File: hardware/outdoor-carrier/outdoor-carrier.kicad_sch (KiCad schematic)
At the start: 49 parts, among them J1 24 VAC, J2 Mode in 24 VAC, J3 XDB307 liquid, J4 XDB307 vapor, J5 XDB307 t.suction, J6 TH1 suction, J7 TH2 liquid, J8 SHT30 FS400, J9 TH3 t.suction, U1 ESP32 DevKit, U2 LM2596HV, U3 ADS1115 0x48, U4 ADS1115 0x49, U5 H11AA1, U6 H11AA1

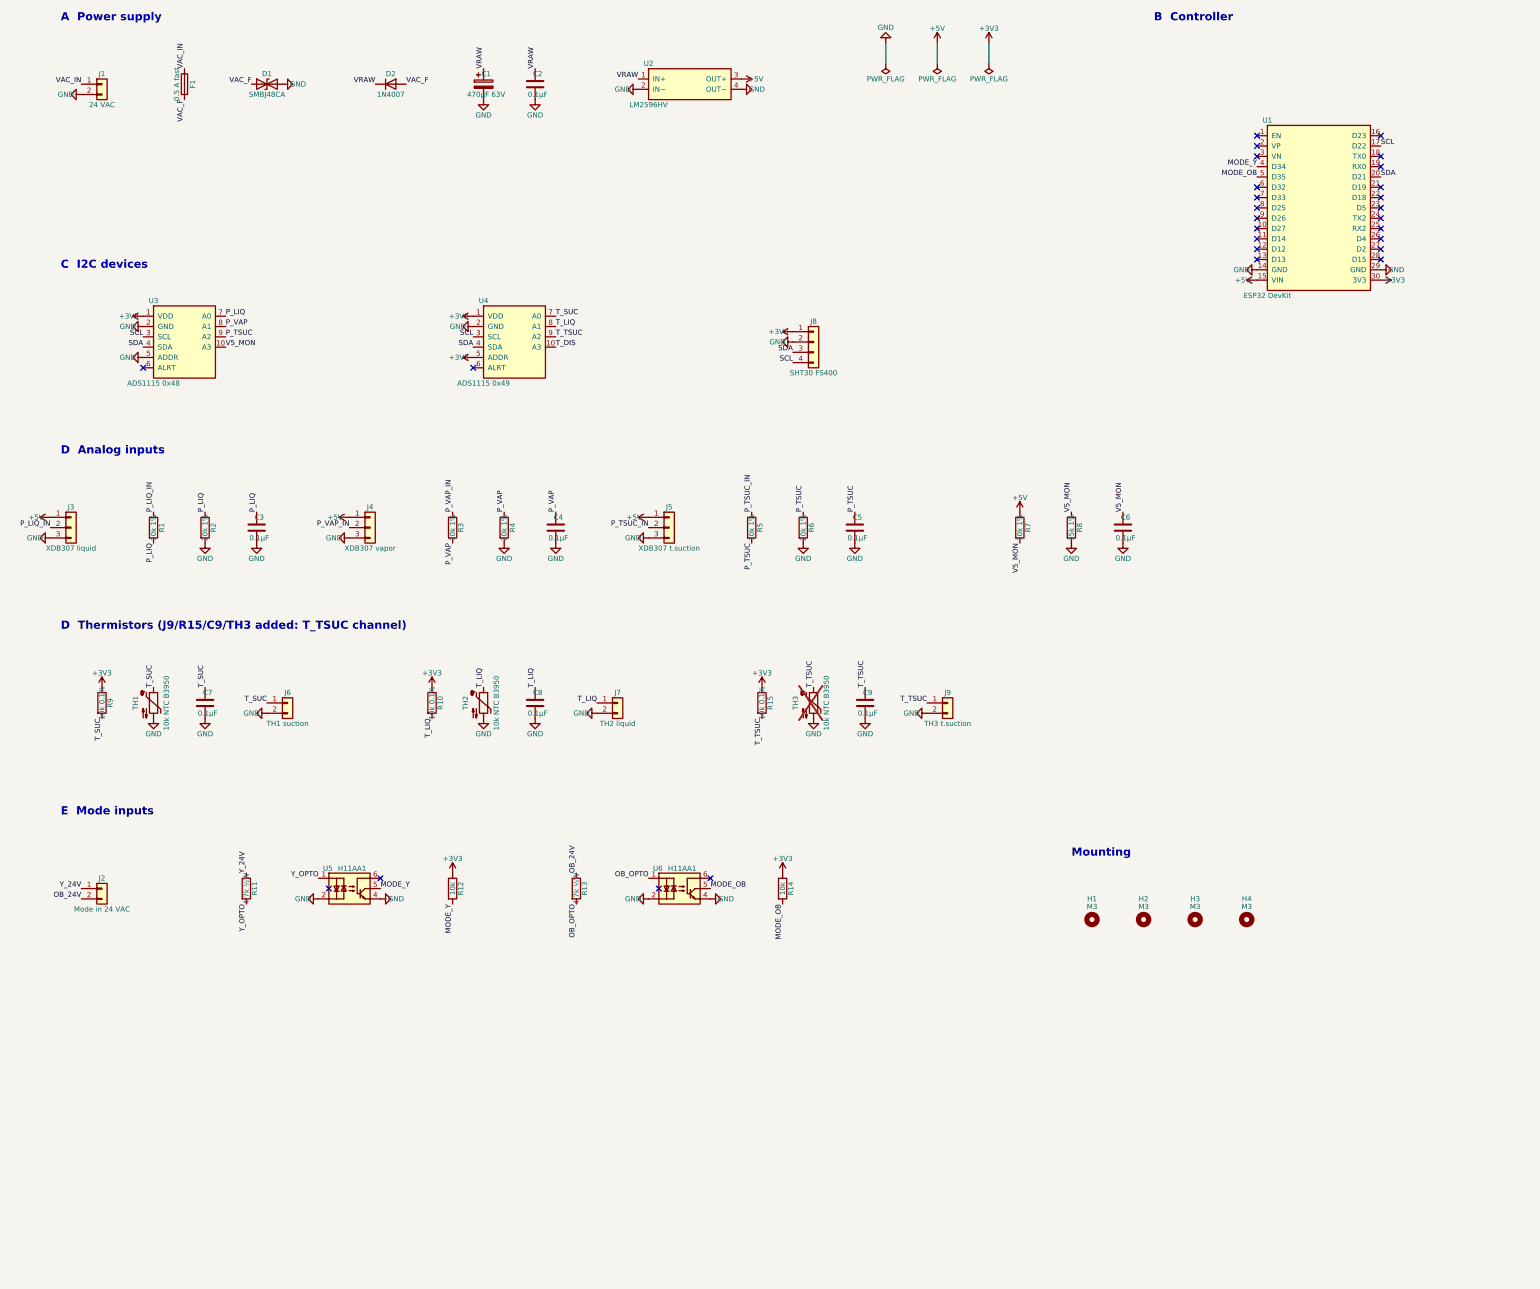
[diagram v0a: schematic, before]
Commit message: Rev B schematics: Wio-SX1262 footprint, flattened AMS1117 symbol, ERC clean
gen_footprints.py: Wio_SX1262 from the Seeed datasheet V1.0 figure 9 (pins 1-8 on
one edge, 12..9 on the other, counter-clockwise; matches design.lora_section and
figure 2). Pads 0.6 x 3.0 mm, 0.8 mm longer outward than the datasheet's 2.2 for hand
soldering; courtyard runs 5 mm past the u.FL side for the plug and pigtail.
gen_sch.py: flatten derived library symbols (AMS1117-3.3 extends AP1117-15), keep
field justification. check_netlist.py: letter pin numbers (audio jack S/T/R) and the
Wio module in the connector summary. design.py: LoRa section spaced out on the sheet.
Checked against KiCad 10: TCA9548APWR pins match MUX_PINS / A0-A2 / RESET / SDA /
SCL / VCC; AudioJack3 S/T/R match the SJ1-3523N pads; AMS1117 1 GND 2 VO 3 VI;
every footprint in design.py exists. ERC 0 errors 0 warnings on both boards.

Co-Authored-By: Claude Opus 5.5 (1M context) <noreply@anthropic.com>
Claude-Session: https://claude.ai/code/session_01V4kWJ9CiBrt94u4WqUxFsk
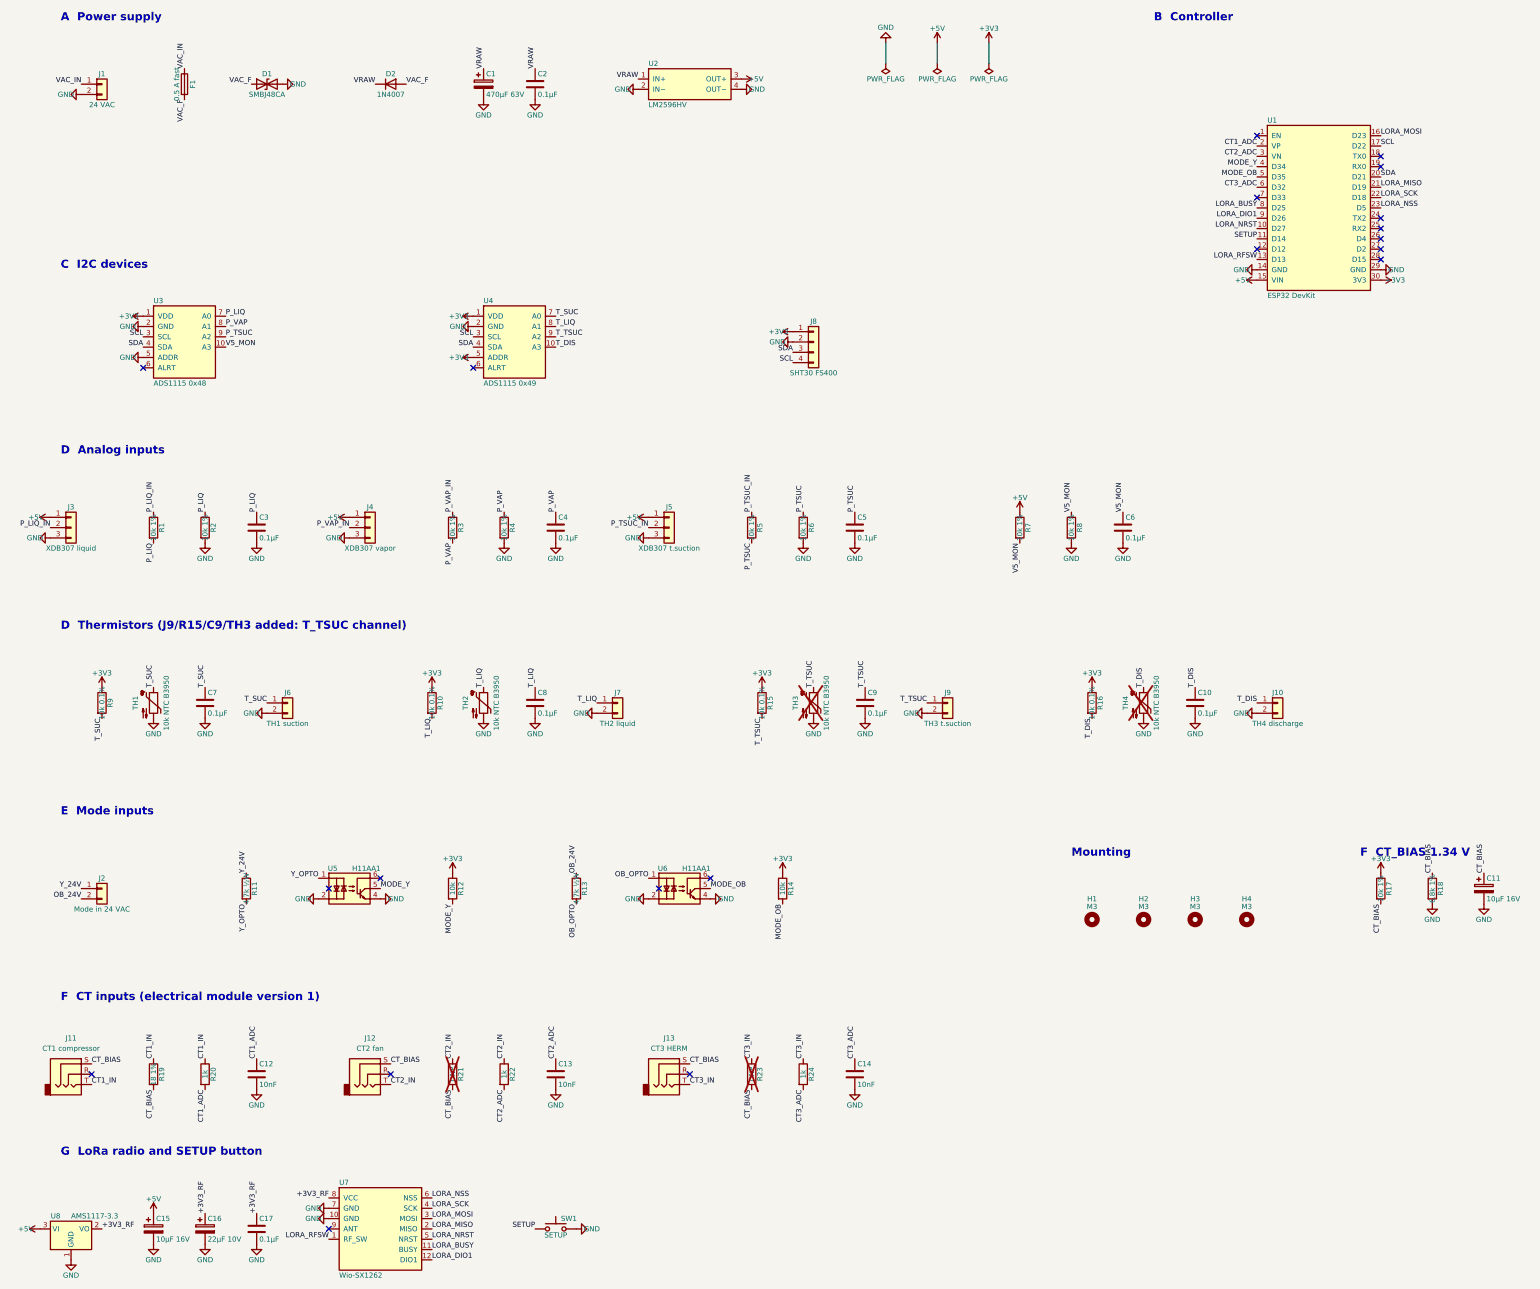
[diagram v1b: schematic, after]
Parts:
- added C10, C17: 0.1µF, Capacitor_THT:C_Disc_D5.0mm_W2.5mm_P2.50mm, symbol Device:C
- added C11, C15: 10µF 16V, Capacitor_THT:CP_Radial_D5.0mm_P2.00mm, symbol Device:C_Polarized
- added C12, C13, C14: 10nF, Capacitor_THT:C_Disc_D5.0mm_W2.5mm_P2.50mm, symbol Device:C
- added C16: 22µF 10V, Capacitor_THT:CP_Radial_D5.0mm_P2.00mm, symbol Device:C_Polarized
- added J10: TH4 discharge, Connector_JST:JST_XH_B2B-XH-A_1x02_P2.50mm_Vertical, symbol Connector_Generic:Conn_01x02
- added J11: CT1 compressor, Connector_Audio:Jack_3.5mm_CUI_SJ1-3523N_Horizontal, symbol Connector_Audio:AudioJack3
- added J12: CT2 fan, Connector_Audio:Jack_3.5mm_CUI_SJ1-3523N_Horizontal, symbol Connector_Audio:AudioJack3
- added J13: CT3 HERM, Connector_Audio:Jack_3.5mm_CUI_SJ1-3523N_Horizontal, symbol Connector_Audio:AudioJack3
- added R16: 10k 0.1%, Resistor_THT:R_Axial_DIN0207_L6.3mm_D2.5mm_P10.16mm_Horizontal, symbol Device:R
- added R17: 10k 1%, Resistor_THT:R_Axial_DIN0207_L6.3mm_D2.5mm_P10.16mm_Horizontal, symbol Device:R
- added R18: 6.8k 1%, Resistor_THT:R_Axial_DIN0207_L6.3mm_D2.5mm_P10.16mm_Horizontal, symbol Device:R
- added R19: 18 1%, Resistor_THT:R_Axial_DIN0207_L6.3mm_D2.5mm_P10.16mm_Horizontal, symbol Device:R
- added R20, R22, R24: 1k, Resistor_THT:R_Axial_DIN0207_L6.3mm_D2.5mm_P10.16mm_Horizontal, symbol Device:R
- added R21, R23: DNP, Resistor_THT:R_Axial_DIN0207_L6.3mm_D2.5mm_P10.16mm_Horizontal, symbol Device:R
- added SW1: SETUP, Button_Switch_THT:SW_PUSH_6mm, symbol Switch:SW_Push
- added TH4: 10k NTC B3950, symbol Device:Thermistor_NTC
- added U7: Wio-SX1262, hvac_carrier:Wio_SX1262, symbol hvac_carrier:Wio_SX1262
- added U8: AMS1117-3.3, Package_TO_SOT_SMD:SOT-223-3_TabPin2, symbol Regulator_Linear:AMS1117-3.3
- R2, R4, R6: value 20k 1% -> 10k 1%
- R8: value 15k 1% -> 10k 1%
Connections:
- net +3V3: now also R16.1, R17.1
- net +5V: now also C15.1, U8.3 (VI)
- net GND: now also C10.2, C11.2, C12.2, C13.2, C14.2, C15.2, C16.2, C17.2, J10.2 (Pin_2), R18.2, SW1.2, TH4.2, U7.10 (GND), U7.7 (GND), U8.1 (GND)
- net T_DIS: now also C10.1, J10.1 (Pin_1), R16.2, TH4.1
- net LORA_NRST: now reaches U1.10 (D27)
- net LORA_NRST: now also U7.5 (NRST)
- net SETUP: now reaches U1.11 (D14)
- net SETUP: now also SW1.1
- net LORA_RFSW: now reaches U1.13 (D13)
- net LORA_RFSW: now also U7.1 (RF_SW)
- net LORA_MOSI: now reaches U1.16 (D23)
- net LORA_MOSI: now also U7.3 (MOSI)
- net CT1_ADC: now reaches U1.2 (VP)
- net CT1_ADC: now also C12.1, R20.2
- net LORA_MISO: now reaches U1.21 (D19)
- net LORA_MISO: now also U7.2 (MISO)
- net LORA_SCK: now reaches U1.22 (D18)
- net LORA_SCK: now also U7.4 (SCK)
- net LORA_NSS: now reaches U1.23 (D5)
- net LORA_NSS: now also U7.6 (NSS)
- net CT2_ADC: now reaches U1.3 (VN)
- net CT2_ADC: now also C13.1, R22.2
- net CT3_ADC: now reaches U1.6 (D32)
- net CT3_ADC: now also C14.1, R24.2
- net LORA_BUSY: now reaches U1.8 (D25)
- net LORA_BUSY: now also U7.11 (BUSY)
- net LORA_DIO1: now reaches U1.9 (D26)
- net LORA_DIO1: now also U7.12 (DIO1)
- new net +3V3_RF: C16.1, C17.1, U7.8 (VCC), U8.2 (VO)
- new net CT1_IN: J11.T, R19.1, R20.1
- new net CT2_IN: J12.T, R21.1, R22.1
- new net CT3_IN: J13.T, R23.1, R24.1
- new net CT_BIAS: C11.1, J11.S, J12.S, J13.S, R17.2, R18.1, R19.2, R21.2, R23.2
- no-connect marks 28 -> 20
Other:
- note added: "F CT inputs (electrical module version 1)"
- note added: "F CT_BIAS 1.34 V"
- note added: "G LoRa radio and SETUP button"

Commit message: Rev B layout: place, route and fab both carrier boards (DRC clean)
Boards: outdoor 110 x 110 mm, indoor 110 x 90 mm (both fit the Hammond 1554R2GY).
The top band is the same on both: the ESP32 (antenna keepout kept), the Wio-SX1262 at
the top edge with its u.FL toward the top wall, the AMS1117 and its caps, SW1 SETUP, and
the rev A power corner moved 10 mm right.
- Outdoor: CT jacks J11-J13 on the left edge. The footprint's own Edge.Cuts nose notch
  is part of the outline, using an edge-silk-trimmed copy in hvac_carrier. The CT
  passives (now 0805) and CT_BIAS sit beside the jacks. The ADS block is next to them,
  with the dividers and thermistor refs in 3.5 mm columns. The mode inputs are on the
  right, and J3-J10 are along the bottom.
- Indoor: TCA9548A, mux jacks J6-J10 along the bottom edge with their pull-ups,
  DS18B20 jacks on the left edge, and J5 on the right edge.
- preroute.py: the rev A hand routes no longer fit, so it is empty. route.py adds
  locked ground fan-out vias for SMD GND pads and a stitching via grid. It fixes
  starved GND thermals (45 degree spokes, then solid) and checks the result with
  kicad-cli. It also fixes a use-after-delete in the duplicate-track pass.
- route-all.sh retries Freerouting until DRC is clean. make_fab.py writes the
  gerbers zip, BOM, renders, schematic PDF, erc.rpt and drc.rpt.
DRC: 0 violations, 0 unconnected, 0 footprint errors (all severities, schematic
parity) on both boards. ERC: 0 errors, 0 warnings.

Co-Authored-By: Claude Opus 5.5 (1M context) <noreply@anthropic.com>
Claude-Session: https://claude.ai/code/session_01V4kWJ9CiBrt94u4WqUxFsk
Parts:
- C12, C13, C14: footprint Capacitor_THT:C_Disc_D5.0mm_W2.5mm_P2.50mm -> Capacitor_SMD:C_0805_2012Metric_Pad1.18x1.45mm_HandSolder
- J11, J12, J13: footprint Connector_Audio:Jack_3.5mm_CUI_SJ1-3523N_Horizontal -> hvac_carrier:Jack_3.5mm_CUI_SJ1-3523N_Horizontal_EdgeTrim
- R17, R18, R19, R20, R21, R22, R23, R24: footprint Resistor_THT:R_Axial_DIN0207_L6.3mm_D2.5mm_P10.16mm_Horizontal -> Resistor_SMD:R_0805_2012Metric_Pad1.20x1.40mm_HandSolder
